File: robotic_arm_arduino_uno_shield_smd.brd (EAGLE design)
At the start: 44.5 x 53.3 mm, 34 parts, among them J1 (ID,OD)=(2.1,5.5)MM, J2 1x06-VERT-MALE, J3 1x06-VERT-MALE, J4 1x08-VERT-MALE, J5 1x08-VERT-MALE

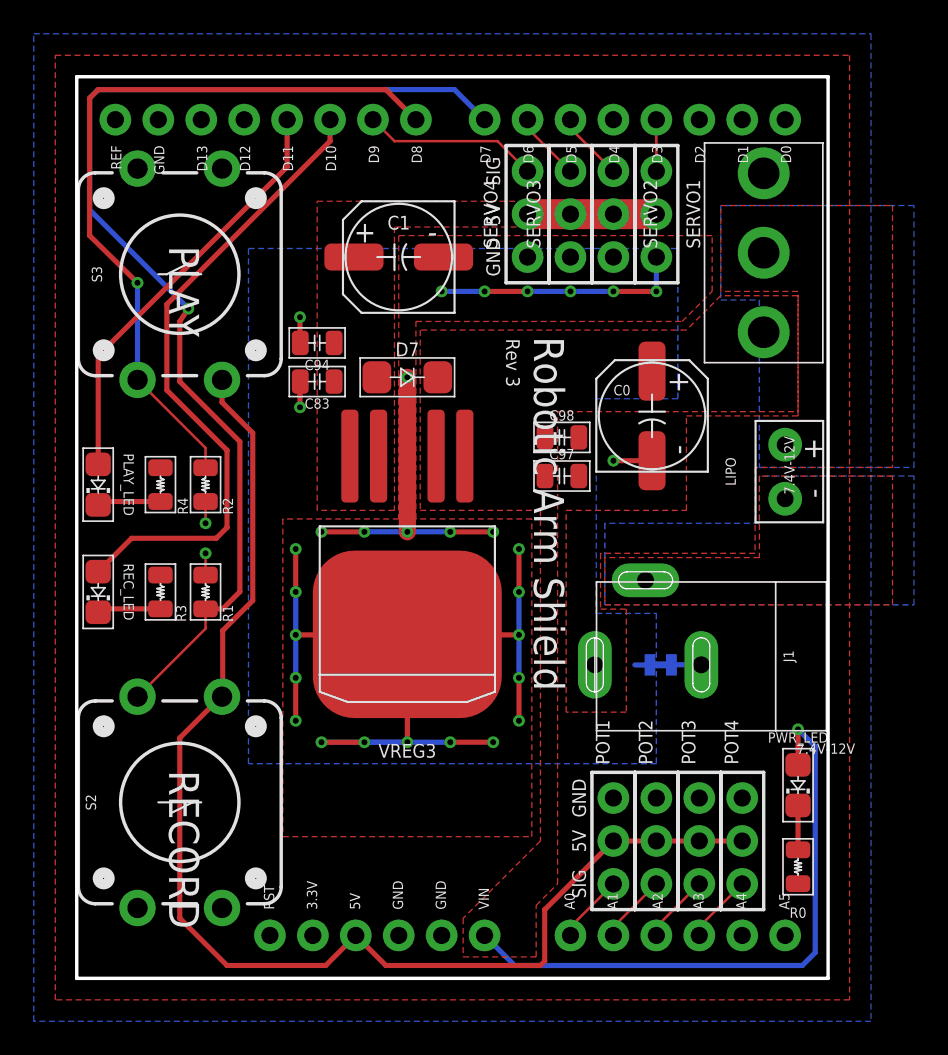
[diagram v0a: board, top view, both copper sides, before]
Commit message: Rev 3:  Adjusted placement of textual elements
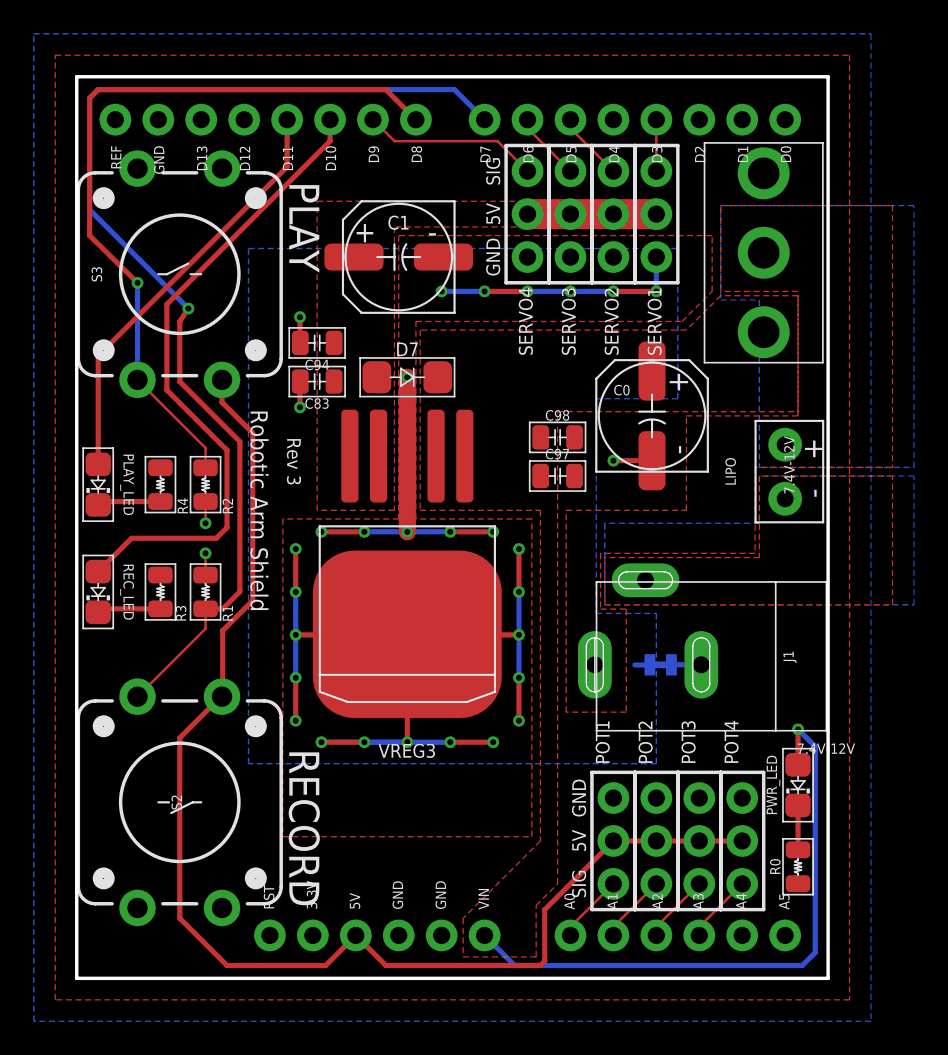
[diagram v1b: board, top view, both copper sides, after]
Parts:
- moved C97 0.25 mm to (28.4, 29.7)
- moved C98 0.25 mm to (28.4, 32.0)
